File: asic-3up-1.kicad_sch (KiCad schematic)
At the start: 66 parts, among them J14 Conn_01x01, J15 Conn_01x01, J5 Conn_01x01, J7 Conn_01x01, U48 MCP1824T-1202E/OT, U49 MCP1824T-1202E/OT, U50 MCP1824T-1202E/OT, U51 MCP1824T-0802E, U52 MCP1824T-0802E, U53 MCP1824T-0802E, U54 BM1362AC_MODE1, U55 BM1362AC_MODE0, U56 BM1362AC_MODE1

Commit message: bumped version to v4. added USB protection diodes for #31. added power TVS diodes for #28. changed snubber resistors to higher wattage and located closer to mosfets for #27 and #30.
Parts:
- C201, C202, C203: DK 1276-1234-1-ND -> 478-KGM05AR71C104KHCT-ND; PARTNO CL05A104KO5NNNC -> KGM05AR71C104KH
- R66: now left out of the parts list
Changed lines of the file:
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@@
 	(title_block
 		(title "emberOne/00")
-		(date "2025-02-25")
-		(rev "3")
+		(date "2025-04-21")
+		(rev "4")
 	)
 	(text "Reference Voltage Regulators"
@@
 			)
 		)
-		(property "DK" "1276-1234-1-ND"
+		(property "DK" "478-KGM05AR71C104KHCT-ND"
 			(at 367.03 73.66 0)
 			(effects
@@
 			)
 		)
-		(property "PARTNO" "CL05A104KO5NNNC"
+		(property "PARTNO" "KGM05AR71C104KH"
 			(at 367.03 73.66 0)
 			(effects
@@
 			)
 		)
-		(property "DK" "1276-1234-1-ND"
+		(property "DK" "478-KGM05AR71C104KHCT-ND"
 			(at 367.03 189.23 0)
 			(effects
@@
 			)
 		)
-		(property "PARTNO" "CL05A104KO5NNNC"
+		(property "PARTNO" "KGM05AR71C104KH"
 			(at 367.03 189.23 0)
 			(effects
@@
 		(unit 1)
 		(exclude_from_sim no)
-		(in_bom yes)
+		(in_bom no)
 		(on_board yes)
 		(dnp yes)
@@
 			)
 		)
-		(property "DK" "1276-1234-1-ND"
+		(property "DK" "478-KGM05AR71C104KHCT-ND"
 			(at 367.03 121.92 0)
 			(effects
@@
 			)
 		)
-		(property "PARTNO" "CL05A104KO5NNNC"
+		(property "PARTNO" "KGM05AR71C104KH"
 			(at 367.03 121.92 0)
 			(effects

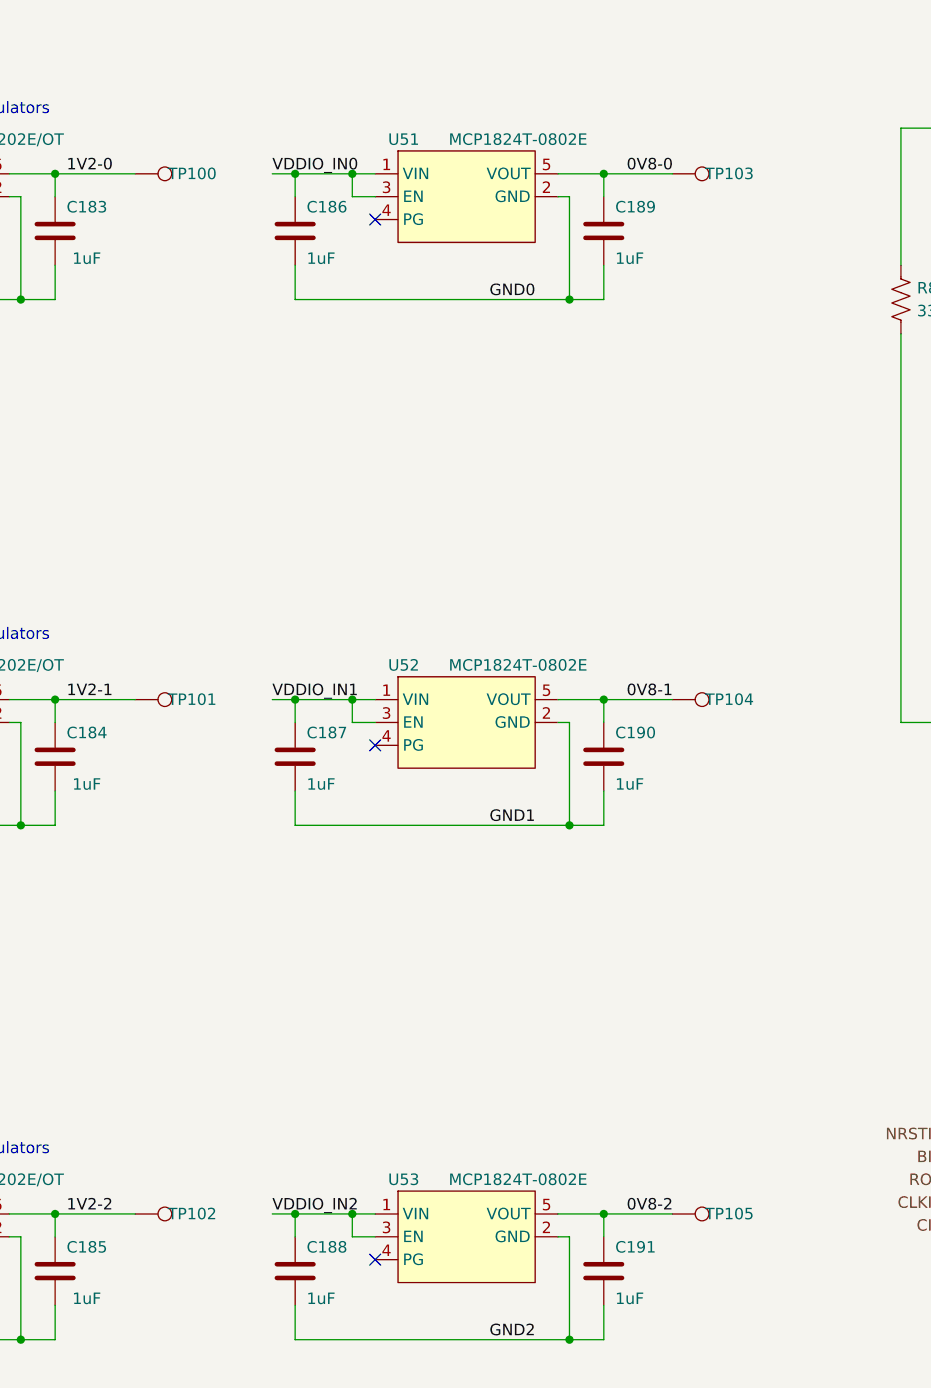
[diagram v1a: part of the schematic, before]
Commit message: added LDO alt part numbers
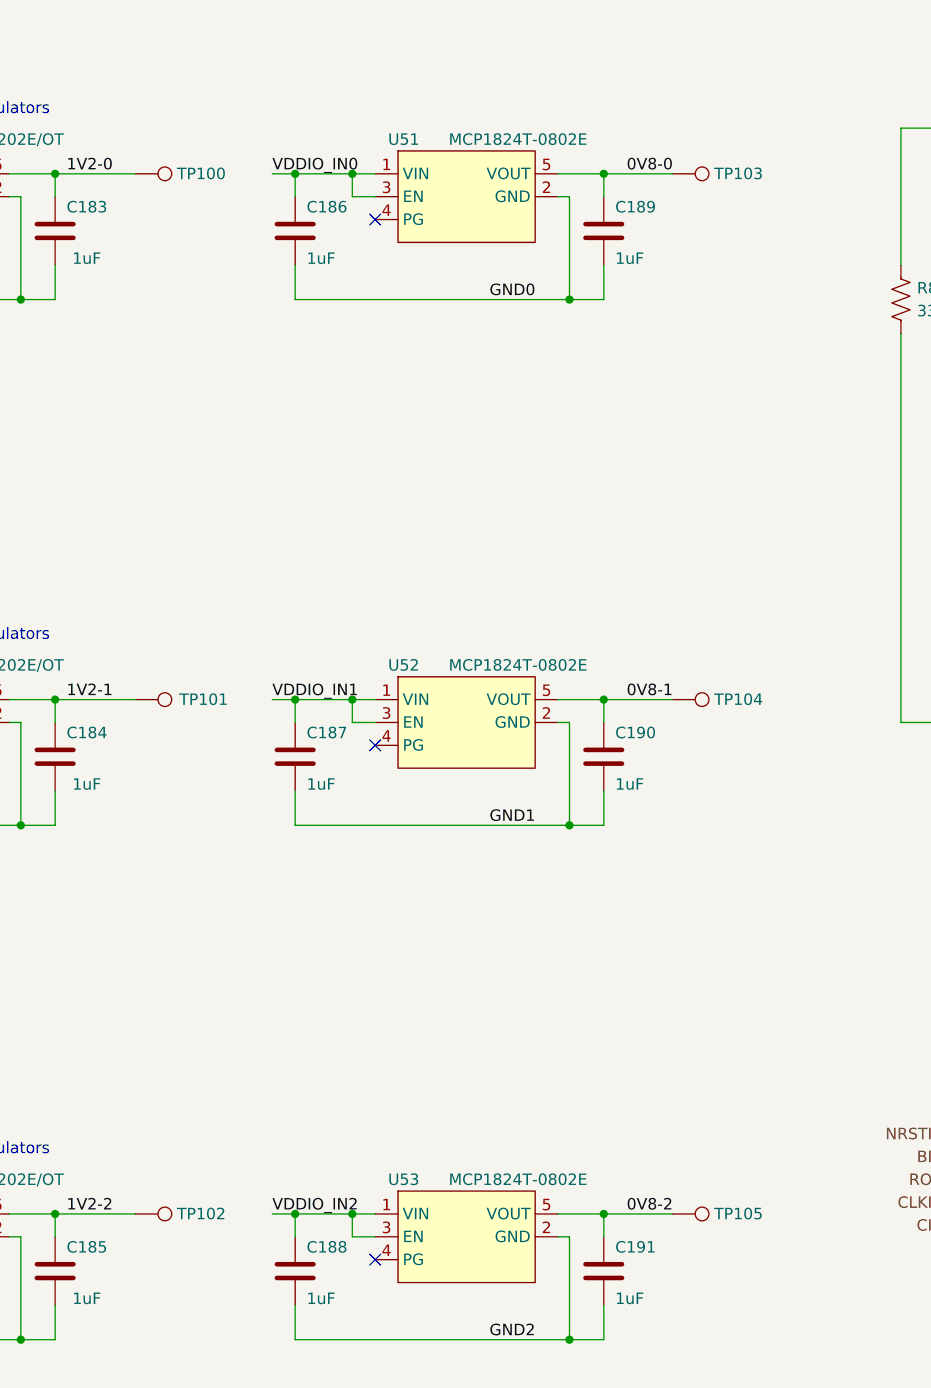
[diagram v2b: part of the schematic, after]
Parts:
- U48, U49, U50: ALT1 (none) -> LDK120M12R
- U51, U52, U53: ALT1 (none) -> LDK120M08R
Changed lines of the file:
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@@
 		(dnp no)
 		(property "Reference" "TP105"
-			(at 166.37 181.61 90)
+			(at 167.386 181.61 90)
 			(effects
 				(font
@@
 		(dnp no)
 		(property "Reference" "TP104"
-			(at 166.37 124.46 90)
+			(at 167.386 124.46 90)
 			(effects
 				(font
@@
 			)
 		)
+		(property "ALT1" "LDK120M08R"
+			(at 137.16 182.88 0)
+			(effects
+				(font
+					(size 1.27 1.27)
+				)
+				(hide yes)
+			)
+		)
 		(pin "1"
 		)
@@
 			)
 		)
+		(property "ALT1" "LDK120M08R"
+			(at 137.16 125.73 0)
+			(effects
+				(font
+					(size 1.27 1.27)
+				)
+				(hide yes)
+			)
+		)
 		(pin "1"
 		)
@@
 			)
 		)
+		(property "ALT1" "LDK120M12R"
+			(at 76.2 67.31 0)
+			(effects
+				(font
+					(size 1.27 1.27)
+				)
+				(hide yes)
+			)
+		)
 		(pin "1"
 		)
@@
 			)
 		)
+		(property "ALT1" "LDK120M12R"
+			(at 76.2 182.88 0)
+			(effects
+				(font
+					(size 1.27 1.27)
+				)
+				(hide yes)
+			)
+		)
 		(pin "1"
 		)
@@
 		(dnp no)
 		(property "Reference" "TP101"
-			(at 106.68 124.46 90)
+			(at 107.95 124.46 90)
 			(effects
 				(font
@@
 			)
 		)
+		(property "ALT1" "LDK120M12R"
+			(at 76.2 125.73 0)
+			(effects
+				(font
+					(size 1.27 1.27)
+				)
+				(hide yes)
+			)
+		)
 		(pin "1"
 		)
@@
 		(dnp no)
 		(property "Reference" "TP100"
-			(at 106.68 66.04 90)
+			(at 107.696 66.04 90)
 			(effects
 				(font
@@
 		(dnp no)
 		(property "Reference" "TP103"
-			(at 166.37 66.04 90)
+			(at 167.386 66.04 90)
 			(effects
 				(font
@@
 		(dnp no)
 		(property "Reference" "TP102"
-			(at 106.68 181.61 90)
+			(at 107.696 181.61 90)
 			(effects
 				(font
@@
 			(at 137.16 67.31 0)
 			(effects
+				(font
+					(size 1.27 1.27)
+				)
+				(hide yes)
+			)
+		)
+		(property "ALT1" "LDK120M08R"
+			(at 137.16 67.31 0)
+			(effects
